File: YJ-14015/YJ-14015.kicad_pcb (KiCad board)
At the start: 2 copper layers, 20.3 x 53.3 mm, 5 parts, among them J1 Conn_01x04, J2 Conn_01x12, U1 YJ-14015, U2 ProMicro

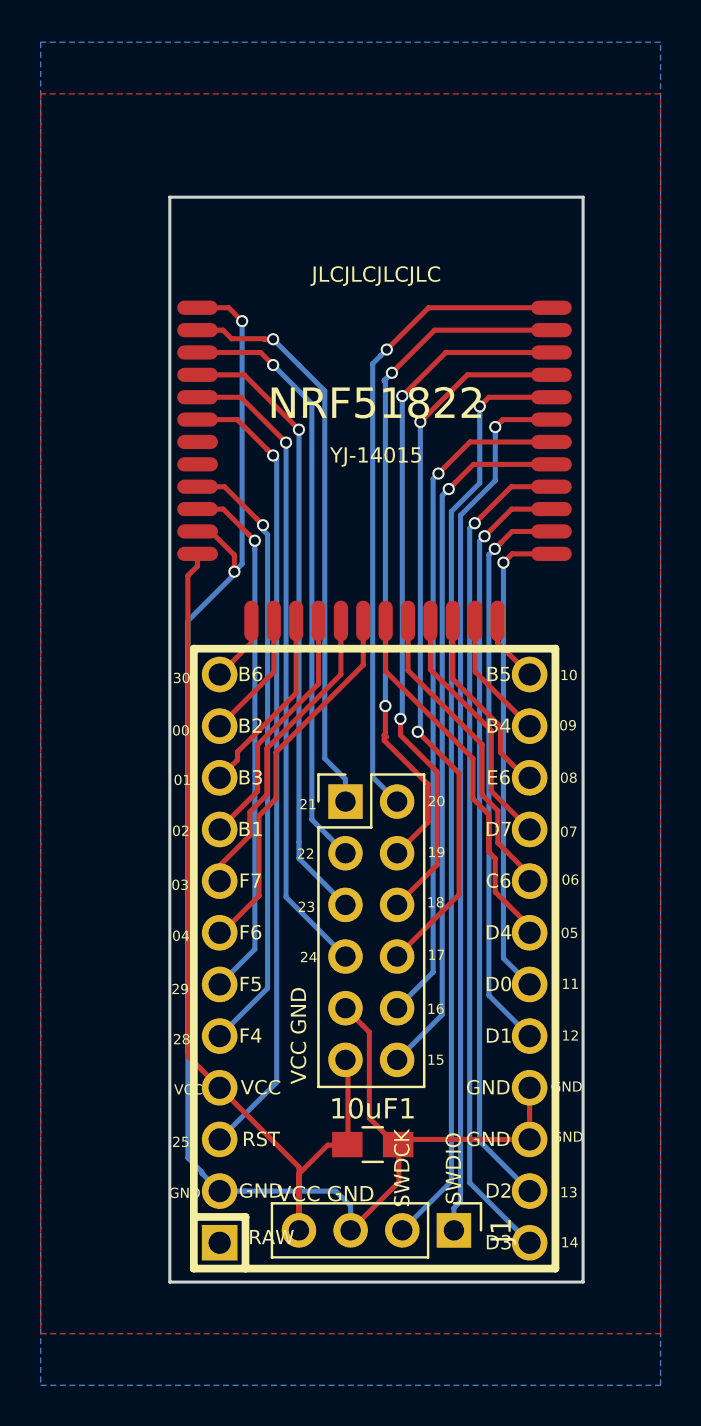
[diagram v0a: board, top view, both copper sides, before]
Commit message: adding battery switch PCB
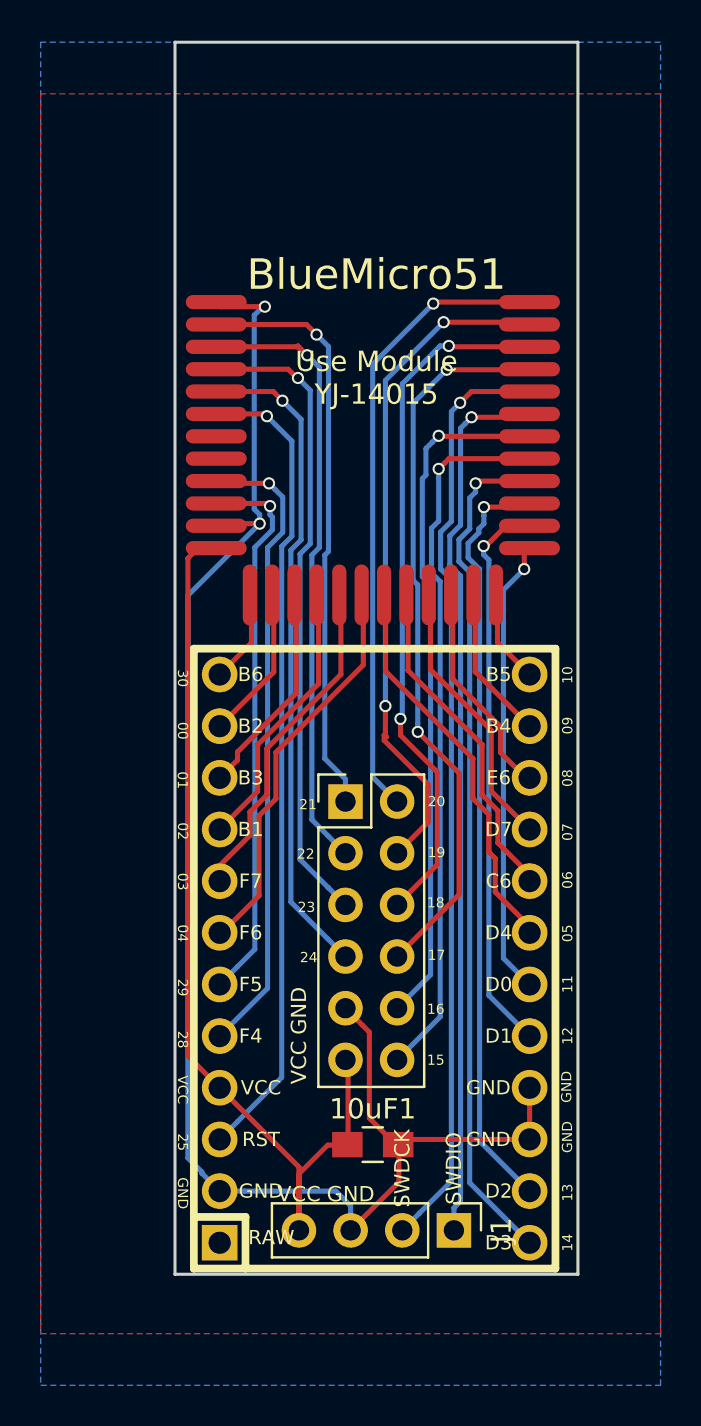
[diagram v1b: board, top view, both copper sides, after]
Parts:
- moved U1 0.29 mm to (148.4, 65.6)
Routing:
- net /P29: track 26.0 -> 27.3 mm
- net /P11: track 23.8 -> 22.5 mm
- net /P28: track 30.2 -> 31.4 mm
- net VCC: track 45.7 -> 46.9 mm
- net /P19: track 34.4 -> 33.3 mm
- net /P23: track 30.4 -> 31.5 mm
- net /P20: track 32.0 -> 31.0 mm
- net /P22: track 29.4 -> 30.2 mm
- net /P25: track 39.3 -> 40.1 mm
- net /P21: track 28.1 -> 28.8 mm
- net /P24: track 31.8 -> 32.5 mm
- net /P14: track 41.2 -> 41.8 mm
- net /P18: track 34.8 -> 34.3 mm
- net GND: track 80.2 -> 80.7 mm
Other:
- board size 20.3 x 53.3 mm -> 19.8 x 60.6 mm
- board text added: "Use Module YJ-14015"
- board text removed: "JLCJLCJLCJLC"
- board text removed: "NRF51822"
- board text removed: "V1.0"
- board text removed: "YJ-14015"
